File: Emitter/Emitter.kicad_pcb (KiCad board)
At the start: 2 copper layers, 5.9 x 14.5 mm, 2 parts, among them J1 Conn_01x02

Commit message: gnd fills
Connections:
- net Net-(D1-K) renamed GND
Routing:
- added copper zone on B.Cu, net GND
- added copper zone on F.Cu, net GND
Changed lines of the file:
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@@
 	)
 	(net 0 "")
-	(net 1 "Net-(D1-K)")
+	(net 1 "GND")
 	(net 2 "Net-(D1-A)")
 	(footprint "Emitter:LED_VSMB2020"
@@
 			(size 1.3208 0.508)
 			(layers "F.Cu" "F.Paste" "F.Mask")
-			(net 1 "Net-(D1-K)")
+			(net 1 "GND")
 			(pinfunction "K")
 			(pintype "passive")
@@
 			(remove_unused_layers no)
 			(roundrect_rratio 0.147059)
-			(net 1 "Net-(D1-K)")
+			(net 1 "GND")
 			(pinfunction "Pin_1")
 			(pintype "passive")
@@
 		(net 2)
 	)
+	(zone
+		(net 1)
+		(net_name "GND")
+		(layers "F&B.Cu")
+		(hatch edge 0.5)
+		(connect_pads
+			(clearance 0.5)
+		)
+		(min_thickness 0.25)
+		(filled_areas_thickness no)
+		(fill yes
+			(thermal_gap 0.5)
+			(thermal_bridge_width 0.5)
+		)
+		(polygon
+			(pts
+				(xy 46.4 76) (xy 63 76) (xy 62.8 97.6) (xy 47.2 96.2)
+			)
+		)
+	)
 )

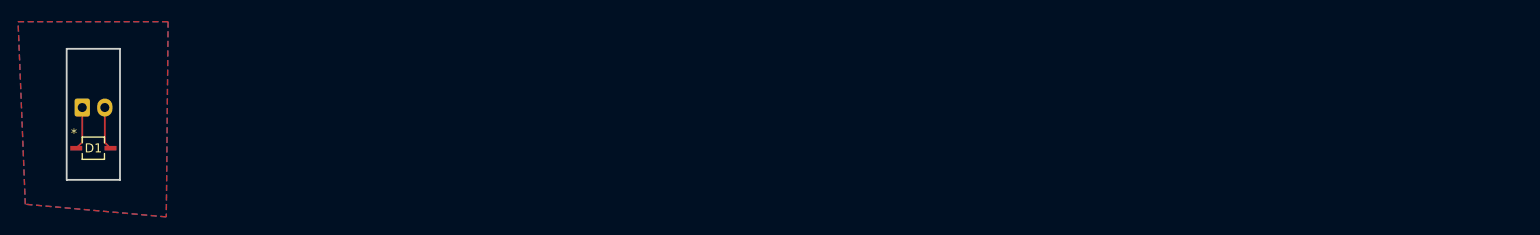
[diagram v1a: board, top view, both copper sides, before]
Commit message: Created Extention for led pcb
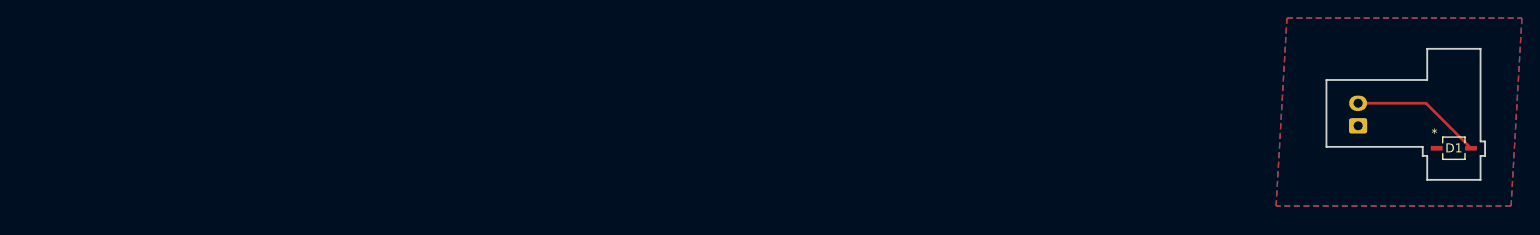
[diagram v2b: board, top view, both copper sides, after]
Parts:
- moved D1 150.5 mm to (205.3, 90.0)
- moved J1 141.2 mm to (194.7, 87.5), turned to 90 degrees
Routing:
- net Net-(D1-A): track 4.76 -> 14.5 mm
- net GND: track 4.77 -> 0.00 mm
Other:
- board size 5.9 x 14.5 mm -> 17.6 x 14.5 mm
